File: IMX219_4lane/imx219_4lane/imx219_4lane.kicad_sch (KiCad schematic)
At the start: 26 parts

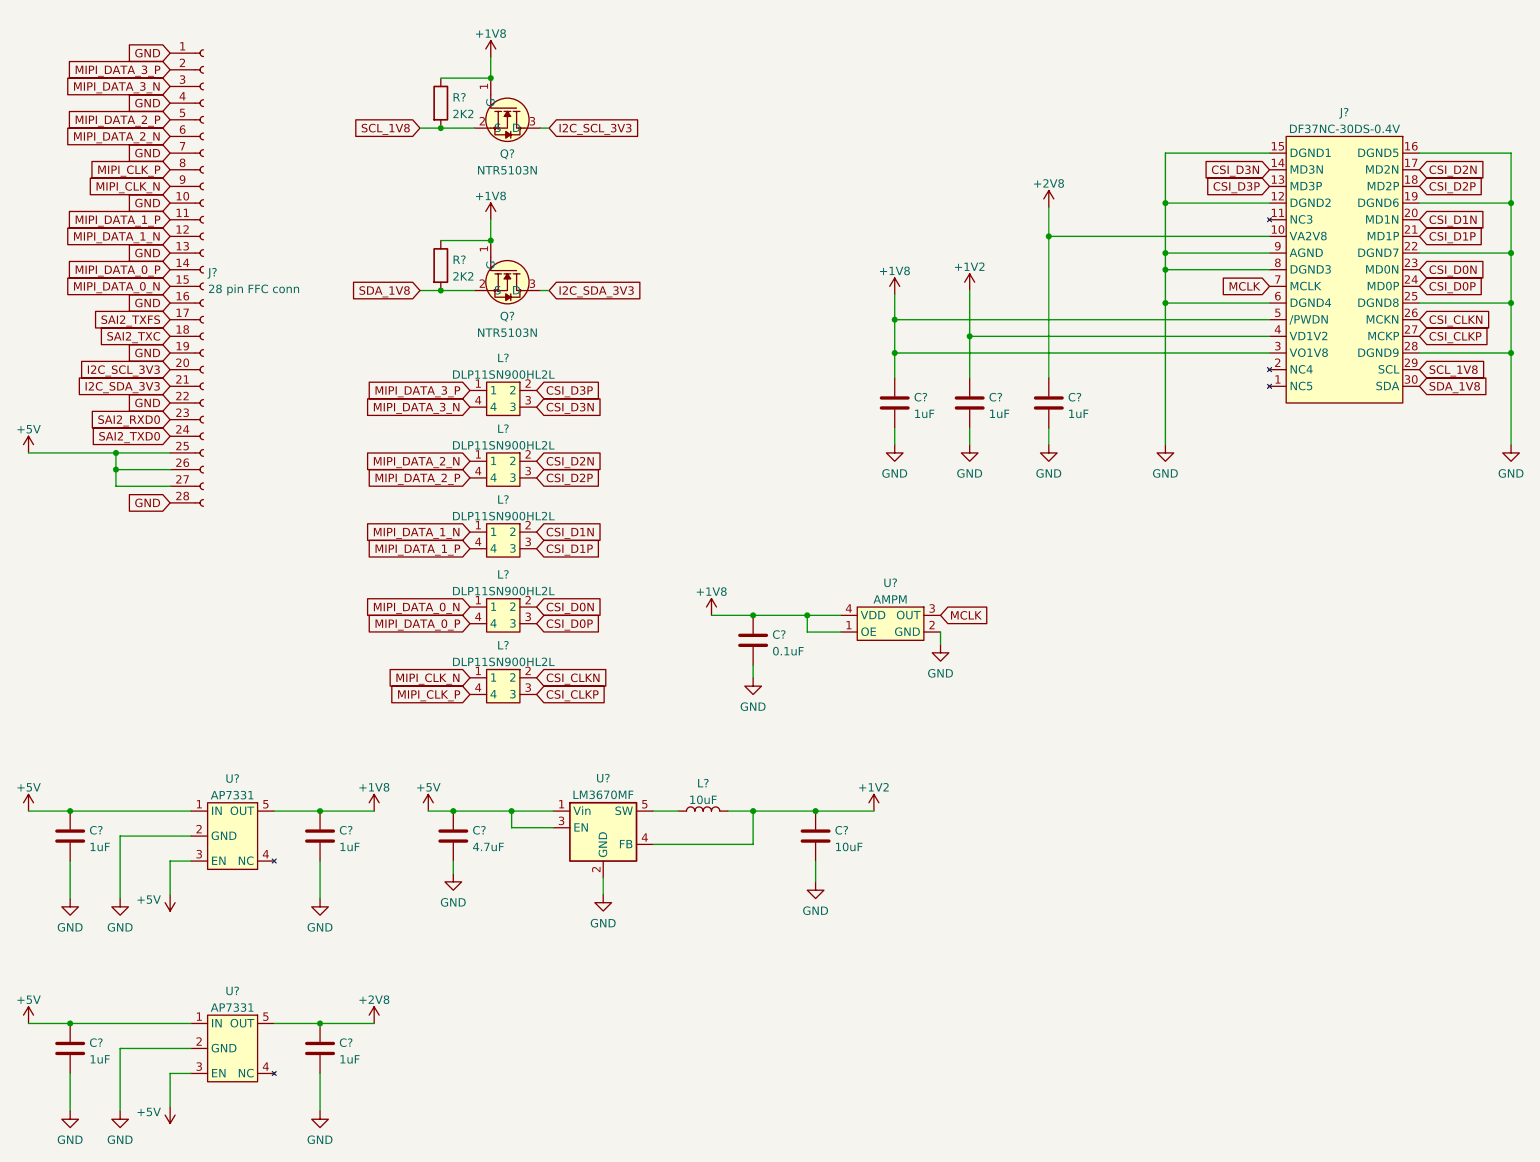
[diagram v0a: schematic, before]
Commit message: new footprint, PCB parts placement
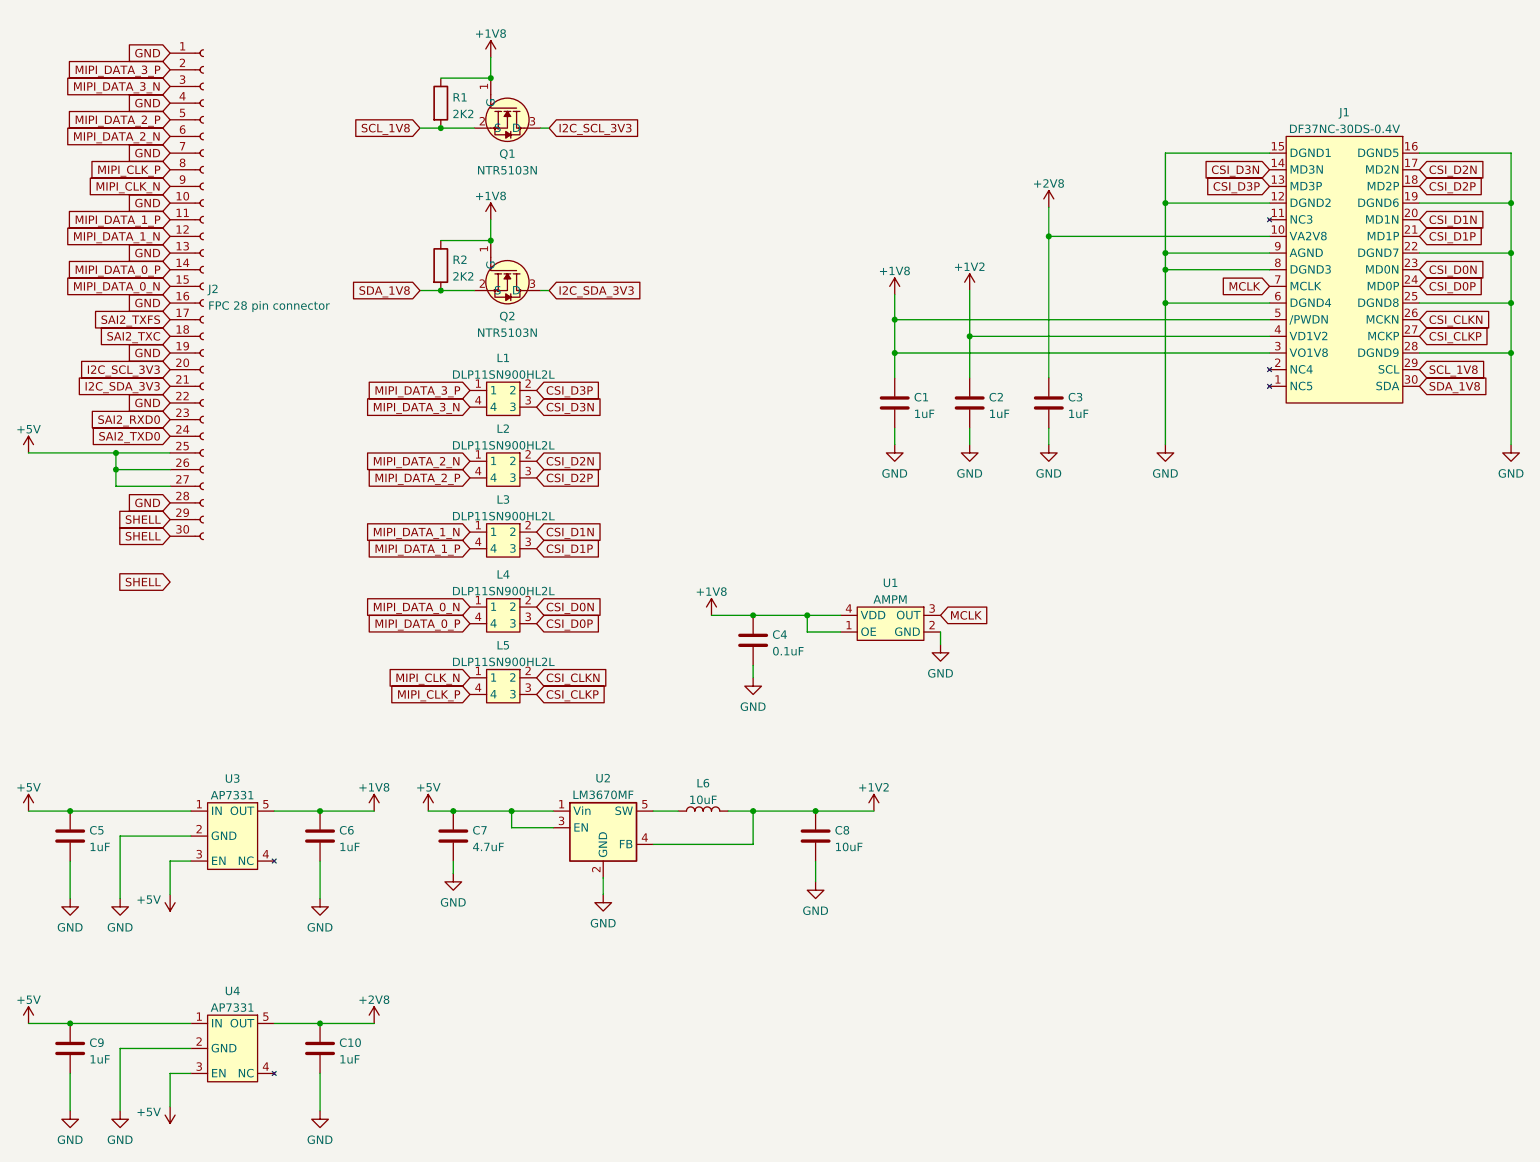
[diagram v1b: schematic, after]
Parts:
- removed J?: 28 pin FFC conn, symbol Connector:Conn_01x28_Female
- added J2: FPC 28 pin connector, unsurv_offline_pcb_footprints:Molex 505110-2891, symbol Connector:Conn_01x30_Female
- C1, C10, C2, C3, C4, C5, C6, C7, C8, C9: renamed from C?; footprint (none) -> Capacitor_SMD:C_0603_1608Metric
- J1: renamed from J?; footprint (none) -> unsurv_offline_pcb_footprints:DF37NC-30DS
- L1, L2, L3, L4, L5: renamed from L?; footprint (none) -> unsurv_offline_pcb_footprints:DLP11SN900HL2L_hand_solder
- L6: renamed from L?; footprint (none) -> Capacitor_SMD:C_0603_1608Metric
- Q1, Q2: renamed from Q?; footprint (none) -> digikey-footprints:SOT-23-3
- R1, R2: renamed from R?; footprint (none) -> Resistor_SMD:R_0603_1608Metric
- U1: renamed from U?; footprint (none) -> unsurv_offline_pcb_footprints:AMPM oscillator
- U2: renamed from U?; footprint Package_TO_SOT_SMD:TSOT-23-5 -> Package_TO_SOT_SMD:SOT-23-5
- U3, U4: renamed from U?; footprint (none) -> Package_TO_SOT_SMD:SOT-23-5
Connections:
- net +5V: now also J2.25 (Pin_25), J2.26 (Pin_26), J2.27 (Pin_27)
- net GND: now also J2.1 (Pin_1), J2.10 (Pin_10), J2.13 (Pin_13), J2.16 (Pin_16), J2.19 (Pin_19), J2.22 (Pin_22), J2.28 (Pin_28), J2.4 (Pin_4), J2.7 (Pin_7)
- net I2C_SCL_3V3: now also J2.20 (Pin_20)
- net I2C_SDA_3V3: now also J2.21 (Pin_21)
- net MIPI_CLK_N: now also J2.9 (Pin_9)
- net MIPI_CLK_P: now also J2.8 (Pin_8)
- net MIPI_DATA_0_N: now also J2.15 (Pin_15)
- net MIPI_DATA_0_P: now also J2.14 (Pin_14)
- net MIPI_DATA_1_N: now also J2.12 (Pin_12)
- net MIPI_DATA_1_P: now also J2.11 (Pin_11)
- net MIPI_DATA_2_N: now also J2.6 (Pin_6)
- net MIPI_DATA_2_P: now also J2.5 (Pin_5)
- net MIPI_DATA_3_N: now also J2.3 (Pin_3)
- net MIPI_DATA_3_P: now also J2.2 (Pin_2)
- net SAI2_RXD0: now also J2.23 (Pin_23)
- net SAI2_TXC: now also J2.18 (Pin_18)
- net SAI2_TXD0: now also J2.24 (Pin_24)
- net SAI2_TXFS: now also J2.17 (Pin_17)
- new net SHELL: J2.29 (Pin_29), J2.30 (Pin_30)

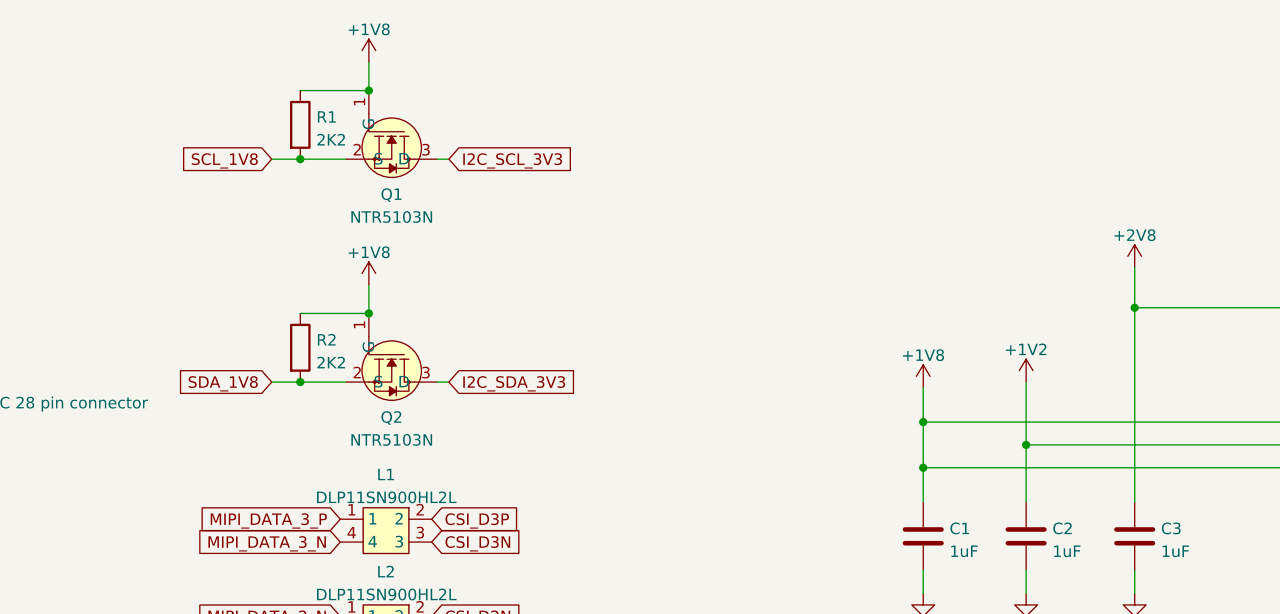
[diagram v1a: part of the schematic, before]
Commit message: added dual channel mosfet for 1v8 I2C
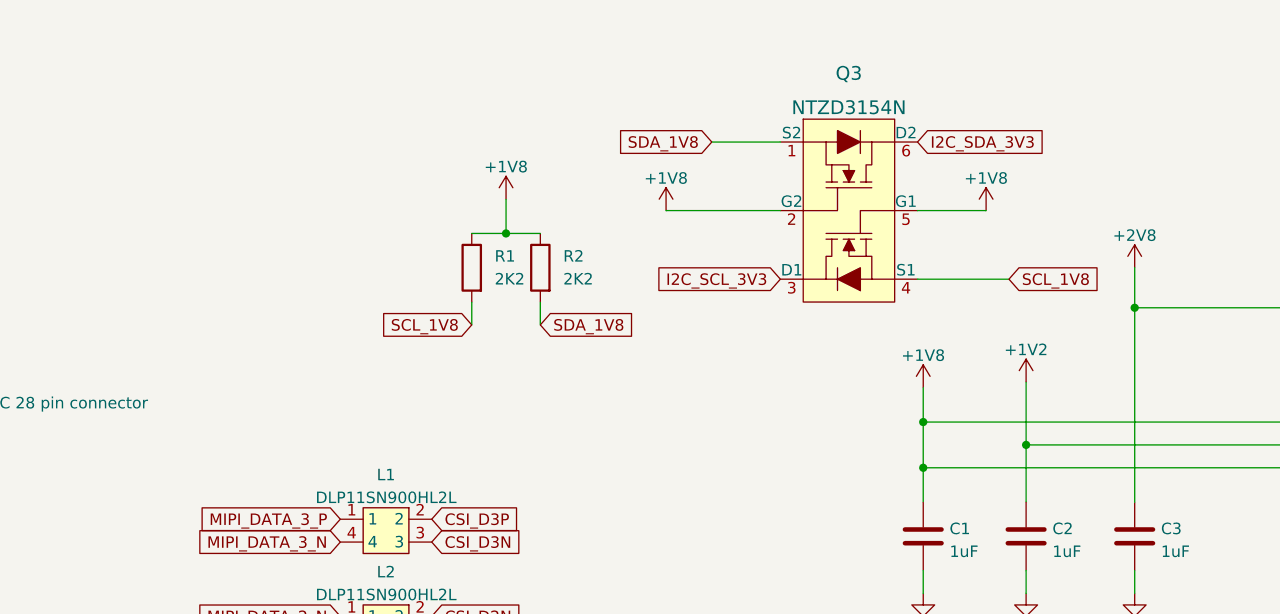
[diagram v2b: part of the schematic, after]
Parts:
- removed Q1, Q2: NTR5103N, digikey-footprints:SOT-23-3, symbol unsurv_offline_pcb_symbols:NTR5103N
- added Q3: NTZD3154N, digikey-footprints:SOT-563, symbol dk_Transistors-FETs-MOSFETs-Arrays:2N7002DW-7-F
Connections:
- net +1V8: now also Q3.2 (G2), Q3.5 (G1)
- net I2C_SCL_3V3: now also Q3.3 (D1)
- net I2C_SDA_3V3: now also Q3.6 (D2)
- net SCL_1V8: now also Q3.4 (S1)
- net SDA_1V8: now also Q3.1 (S2)

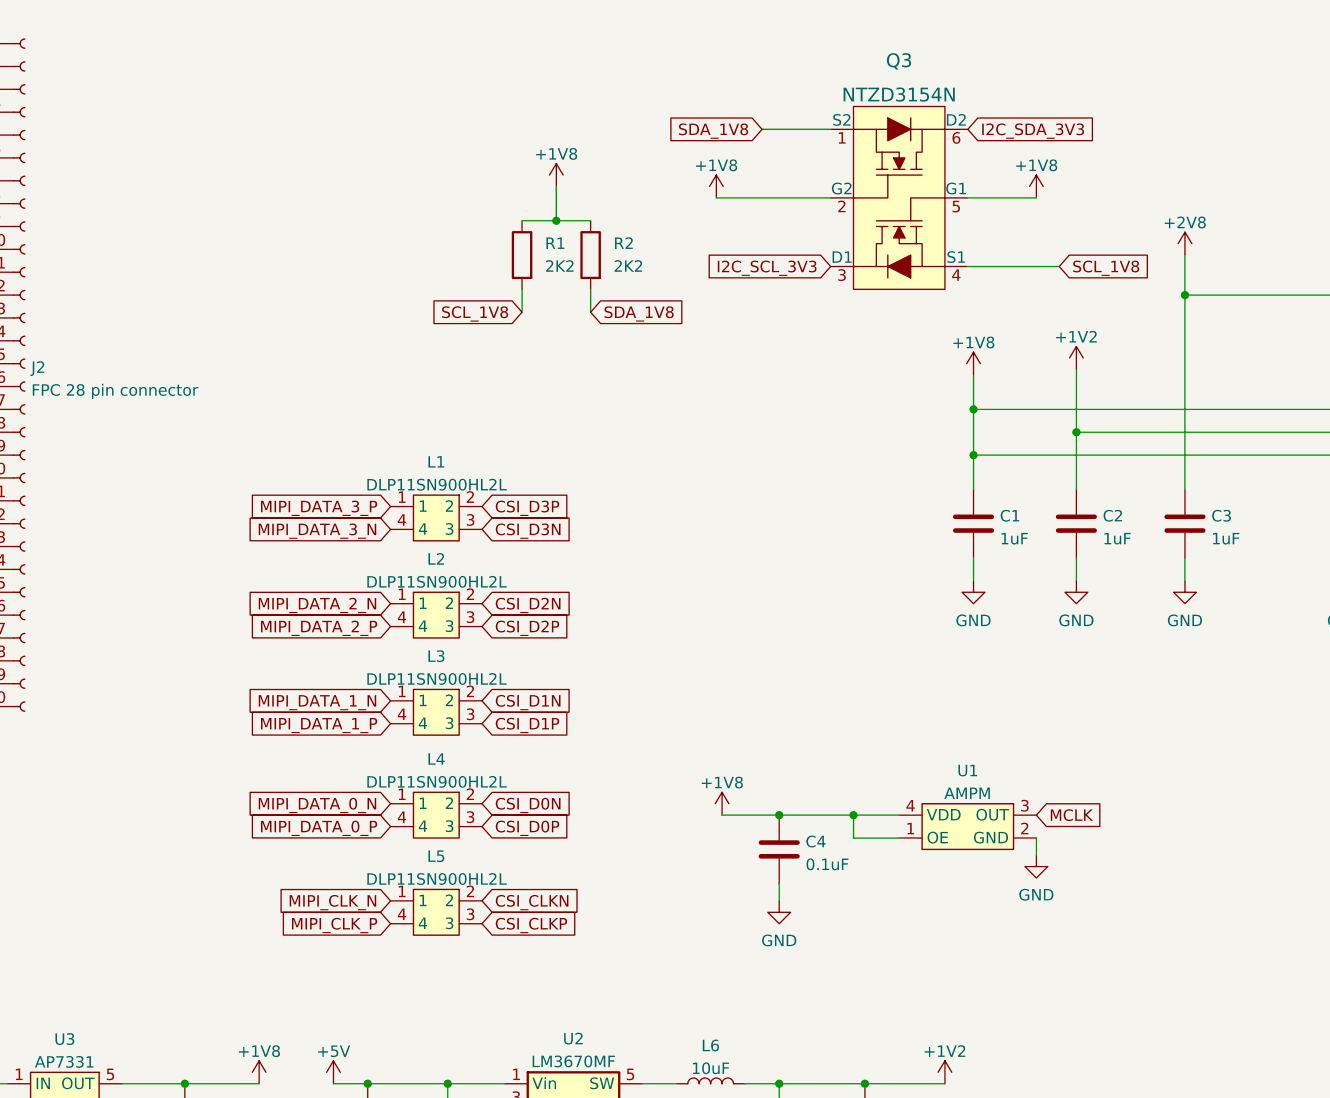
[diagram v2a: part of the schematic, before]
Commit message: length matching mipi signals
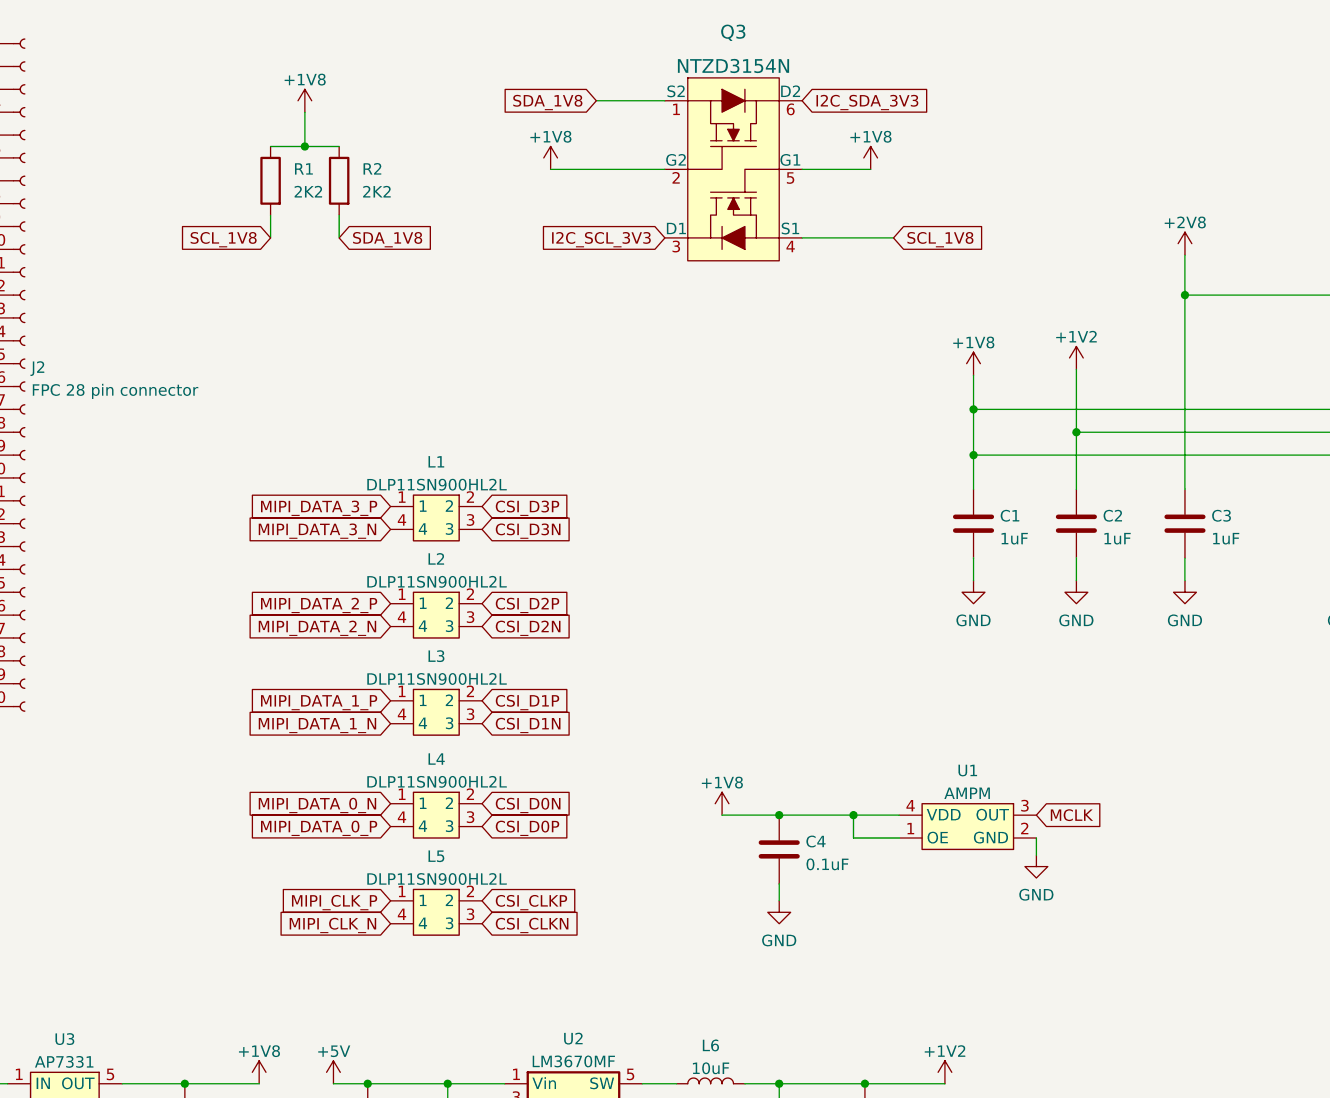
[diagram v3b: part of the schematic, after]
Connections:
- net CSI_CLKN: now also L5.3; no longer L5.2
- net CSI_CLKP: now also L5.2; no longer L5.3
- net CSI_D1N: now also L3.3; no longer L3.2
- net CSI_D1P: now also L3.2; no longer L3.3
- net CSI_D2N: now also L2.3; no longer L2.2
- net CSI_D2P: now also L2.2; no longer L2.3
- net MIPI_CLK_N: now also L5.4; no longer L5.1
- net MIPI_CLK_P: now also L5.1; no longer L5.4
- net MIPI_DATA_1_N: now also L3.4; no longer L3.1
- net MIPI_DATA_1_P: now also L3.1; no longer L3.4
- net MIPI_DATA_2_N: now also L2.4; no longer L2.1
- net MIPI_DATA_2_P: now also L2.1; no longer L2.4
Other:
- moved on the sheet: Q3, R1, R2

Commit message: prototype routing
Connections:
- net CSI_D0N: now also L4.3; no longer L4.2
- net CSI_D0P: now also L4.2; no longer L4.3
- net MIPI_DATA_0_N: now also L4.4; no longer L4.1
- net MIPI_DATA_0_P: now also L4.1; no longer L4.4
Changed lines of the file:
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@@
     )
   )
-  (global_label "CSI_D0N" (shape input) (at 99.695 102.87 0) (fields_autoplaced)
-    (effects (font (size 1.27 1.27)) (justify left))
-    (property "Intersheet References" "${INTERSHEET_REFS}" (id 0) (at 109.97 102.7906 0)
-      (effects (font (size 1.27 1.27)) (justify left) hide)
-    )
-  )
-  (global_label "CSI_D0P" (shape input) (at 99.695 105.41 0) (fields_autoplaced)
-    (effects (font (size 1.27 1.27)) (justify left))
-    (property "Intersheet References" "${INTERSHEET_REFS}" (id 0) (at 109.9095 105.3306 0)
+  (global_label "CSI_D0N" (shape input) (at 99.695 105.41 0) (fields_autoplaced)
+    (effects (font (size 1.27 1.27)) (justify left))
+    (property "Intersheet References" "${INTERSHEET_REFS}" (id 0) (at 109.97 105.3306 0)
+      (effects (font (size 1.27 1.27)) (justify left) hide)
+    )
+  )
+  (global_label "CSI_D0P" (shape input) (at 99.695 102.87 0) (fields_autoplaced)
+    (effects (font (size 1.27 1.27)) (justify left))
+    (property "Intersheet References" "${INTERSHEET_REFS}" (id 0) (at 109.9095 102.7906 0)
       (effects (font (size 1.27 1.27)) (justify left) hide)
     )
@@
     )
   )
-  (global_label "MIPI_DATA_0_P" (shape input) (at 89.535 105.41 180) (fields_autoplaced)
-    (effects (font (size 1.27 1.27)) (justify right))
-    (property "Intersheet References" "${INTERSHEET_REFS}" (id 0) (at 73.3938 105.3306 0)
+  (global_label "MIPI_DATA_0_P" (shape input) (at 89.535 102.87 180) (fields_autoplaced)
+    (effects (font (size 1.27 1.27)) (justify right))
+    (property "Intersheet References" "${INTERSHEET_REFS}" (id 0) (at 73.3938 102.7906 0)
       (effects (font (size 1.27 1.27)) (justify right) hide)
     )
@@
     )
   )
-  (global_label "MIPI_DATA_0_N" (shape input) (at 89.535 102.87 180) (fields_autoplaced)
-    (effects (font (size 1.27 1.27)) (justify right))
-    (property "Intersheet References" "${INTERSHEET_REFS}" (id 0) (at 73.3333 102.7906 0)
-      (effects (font (size 1.27 1.27)) (justify right) hide)
-    )
+  (global_label "MIPI_DATA_0_N" (shape input) (at 89.535 105.41 180) (fields_autoplaced)
+    (effects (font (size 1.27 1.27)) (justify right))
+    (property "Intersheet References" "${INTERSHEET_REFS}" (id 0) (at 73.3333 105.3306 0)
+      (effects (font (size 1.27 1.27)) (justify right) hide)
+    )
